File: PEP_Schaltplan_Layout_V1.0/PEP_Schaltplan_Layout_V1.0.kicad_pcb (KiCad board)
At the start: 2 copper layers, 202.5 x 119.7 mm, 115 parts, among them Q1 BC546, Q2 BC556, SW1 SW_DIP_x04, SW10 SW_DIP_x04, SW11 SW_DIP_x04, SW12 SW_DIP_x04, SW13 SW_DIP_x04, SW14 SW_DIP_x04, SW15 SW_DIP_x04, SW16 SW_DIP_x04, SW2 SW_DIP_x04, SW3 SW_DIP_x04, SW4 SW_DIP_x04, SW5 SW_DIP_x04, SW6 SW_DIP_x04, SW7 SW_DIP_x04, SW8 SW_DIP_x04, SW9 SW_DIP_x04, U1 AD822ANZ_new, U2 LM7805_TO220, U3 LM7905_TO220, U4 LT1819, U5 LT1819, U6 LT1819, U7 LT1819

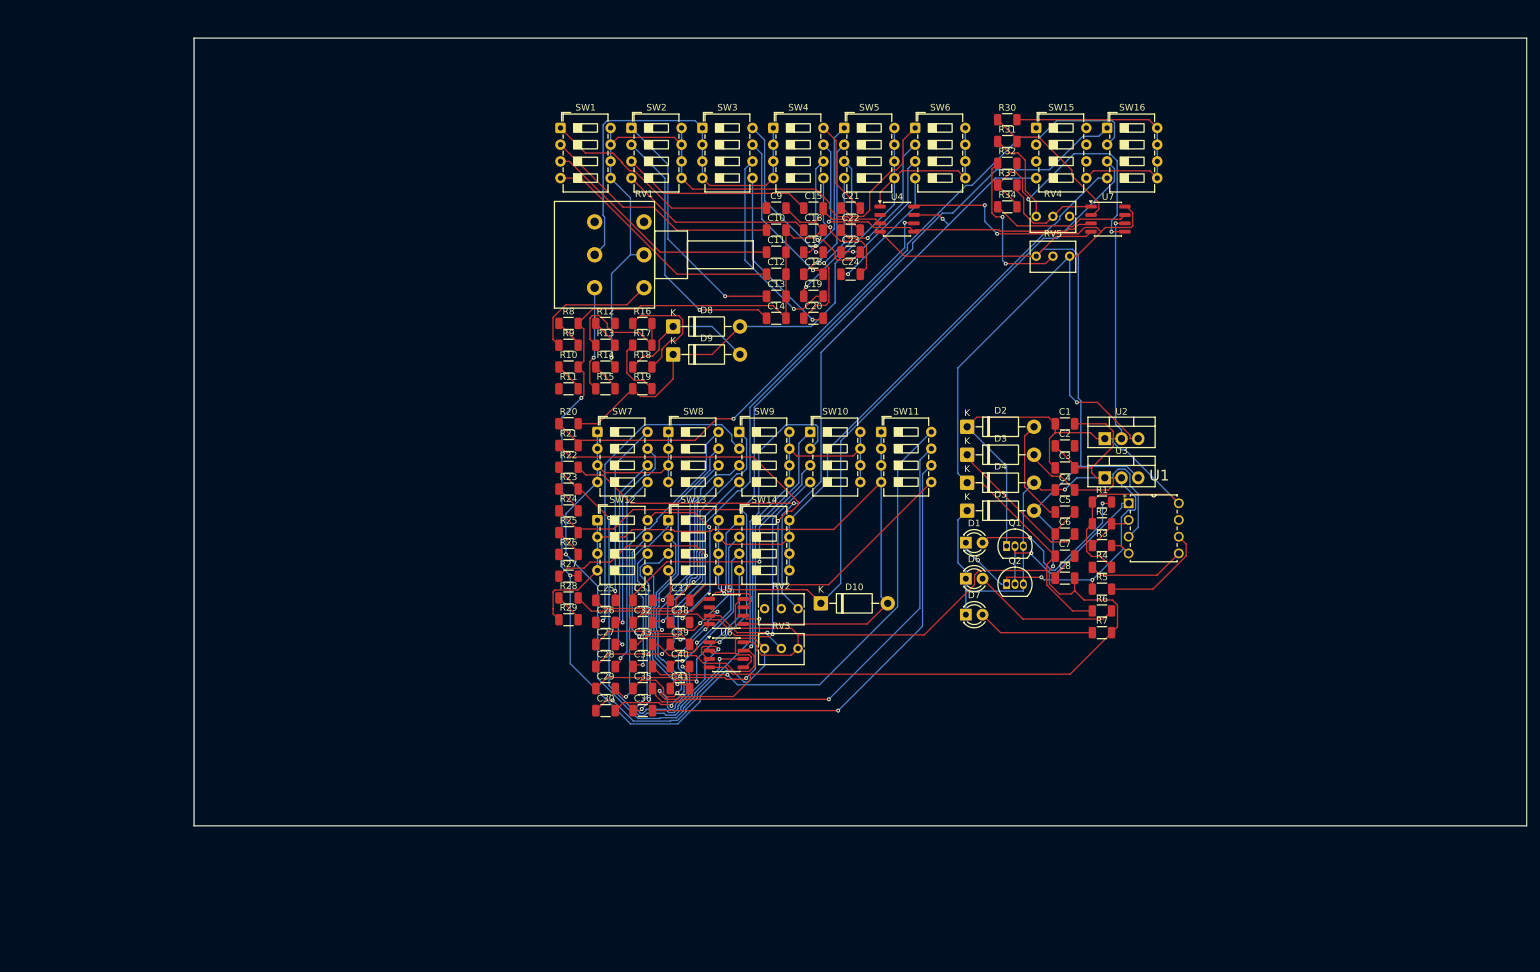
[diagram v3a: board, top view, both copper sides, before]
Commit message: Pinheads eingefügt, GND überall (hoffentlich angebunden)
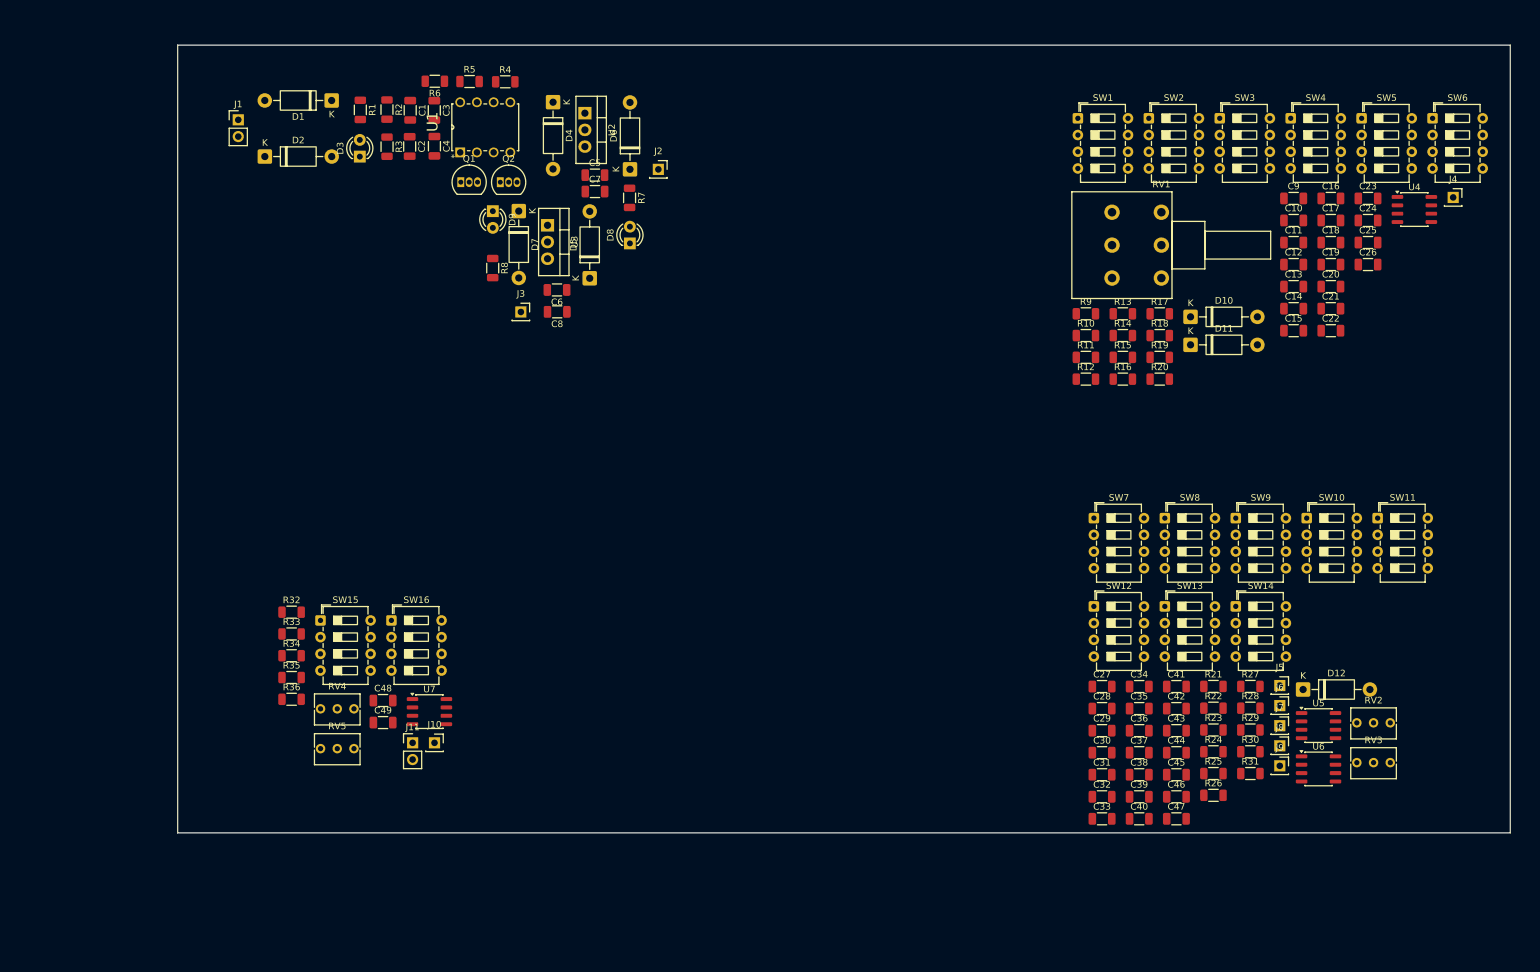
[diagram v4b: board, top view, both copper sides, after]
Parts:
- added C42: 220p, Capacitor_SMD:C_1206_3216Metric, F.Cu at (198.0, 142.6)
- added C43: 47p, Capacitor_SMD:C_1206_3216Metric, F.Cu at (198.0, 145.9)
- added C44: 47p, Capacitor_SMD:C_1206_3216Metric, F.Cu at (198.0, 149.3)
- added C45: 22p, Capacitor_SMD:C_1206_3216Metric, F.Cu at (198.0, 152.6)
- added C46: 0, Capacitor_SMD:C_1206_3216Metric, F.Cu at (198.0, 156.0)
- added C47: 0, Capacitor_SMD:C_1206_3216Metric, F.Cu at (198.0, 159.3)
- added C48: 100n, Capacitor_SMD:C_1206_3216Metric, F.Cu at (77.4, 141.3)
- added C49: 100n, Capacitor_SMD:C_1206_3216Metric, F.Cu at (77.4, 144.7)
- added D11: 1N4148, Diode_THT:D_DO-41_SOD81_P10.16mm_Horizontal, F.Cu at (200.2, 87.3)
- added D12: 1N4148, Diode_THT:D_DO-41_SOD81_P10.16mm_Horizontal, F.Cu at (217.3, 139.7)
- added J1: Conn_01x02_Pin, Connector_PinHeader_2.54mm:PinHeader_1x02_P2.54mm_Vertical, F.Cu at (55.4, 53.1)
- added J10: Conn_01x01_Pin, Connector_PinSocket_2.54mm:PinSocket_1x01_P2.54mm_Vertical, F.Cu at (85.3, 147.8)
- added J11: Conn_01x02_Pin, Connector_PinHeader_2.54mm:PinHeader_1x02_P2.54mm_Vertical, F.Cu at (81.9, 147.8)
- added J2: Conn_01x01_Pin, Connector_PinSocket_2.54mm:PinSocket_1x01_P2.54mm_Vertical, F.Cu at (119.3, 60.6)
- added J3: Conn_01x01_Pin, Connector_PinSocket_2.54mm:PinSocket_1x01_P2.54mm_Vertical, F.Cu at (98.4, 82.3)
- added J4: Conn_01x01_Pin, Connector_PinSocket_2.54mm:PinSocket_1x01_P2.54mm_Vertical, F.Cu at (240.1, 64.9)
- added J5: Conn_01x01_Pin, Connector_PinSocket_2.54mm:PinSocket_1x01_P2.54mm_Vertical, F.Cu at (213.7, 139.1)
- added J6: Conn_01x01_Pin, Connector_PinSocket_2.54mm:PinSocket_1x01_P2.54mm_Vertical, F.Cu at (213.7, 142.1)
- added J7: Conn_01x01_Pin, Connector_PinSocket_2.54mm:PinSocket_1x01_P2.54mm_Vertical, F.Cu at (213.7, 145.2)
- added J8: Conn_01x01_Pin, Connector_PinSocket_2.54mm:PinSocket_1x01_P2.54mm_Vertical, F.Cu at (213.7, 148.2)
- added J9: Conn_01x01_Pin, Connector_PinSocket_2.54mm:PinSocket_1x01_P2.54mm_Vertical, F.Cu at (213.7, 151.3)
- added R35: 10k, Resistor_SMD:R_1206_3216Metric, F.Cu at (63.5, 137.8)
- added R36: 10k, Resistor_SMD:R_1206_3216Metric, F.Cu at (63.5, 141.1)
- C10, C9: value 6.8n -> 100n
- C25: value 22n -> 6.8n
- C26: value 4.7n -> 6.8n
- C27: value 470p -> 100n
- C28: value 100p -> 100n
- C29: value 47p -> 100n
- C30: value 22p -> 100n
- C31: value 0 -> 22n
- C32, C40: value 0 -> 4.7n
- C33: value 1µ -> 470p
- C34: value 4.7n -> 100p
- C35: value 1n -> 47p
- C36: value 220p -> 22p
- C37, C38: value 47p -> 0
- C39: value 22p -> 1µ
- C41: value 0 -> 1n
- D1, D6, D7: value LED -> 1N4002; footprint LED_THT:LED_D3.0mm -> Diode_THT:D_DO-41_SOD81_P10.16mm_Horizontal
- D3: value 1N4002 -> LED; footprint Diode_THT:D_DO-41_SOD81_P10.16mm_Horizontal -> LED_THT:LED_D3.0mm
- D8, D9: value 1N4148 -> LED; footprint Diode_THT:D_DO-41_SOD81_P10.16mm_Horizontal -> LED_THT:LED_D3.0mm
- R11, R13: value 10k -> 0
- R12, R24: value 0 -> 10k
- R14: value 500 -> 10k
- R15, R9: value 0 -> 500
- R16: value 24K -> 0
- R17: value 12k -> 24K
- R18: value 0 -> 12k
- R20: value 1k -> 0
- R22, R32, R33: value 10k -> 1k
- R23: value 190k -> 0R
- R25: value 0 -> 190k
- R26: value 18k -> 0
- R27: value 100k -> 0
- R28: value 12k -> 18k
- R29: value ^0 -> 100k
- R30: value 1k -> 12k
- R31: value 1k -> ^0
- R6: value 470 -> 10k
- R8: value 500 -> 470
- moved RV4 132.0 mm to (73.0, 142.6)
- moved RV5 132.0 mm to (73.0, 148.6)
- moved SW16 132.0 mm to (78.7, 129.2)
- moved SW15 132.0 mm to (67.9, 129.2)
- moved R6 129.5 mm to (85.3, 47.2), turned to 180 degrees
- moved R32 128.4 mm to (63.5, 127.9)
- moved R33 128.4 mm to (63.5, 131.2)
- moved R34 128.4 mm to (63.5, 134.5)
- moved C25 128.0 mm to (227.1, 71.7)
- moved C26 128.0 mm to (227.1, 75.1)
- moved R1 127.5 mm to (74.0, 51.6), turned to -90 degrees
- moved U7 127.4 mm to (84.5, 143.0)
- moved R2 125.6 mm to (78.0, 51.5), turned to -90 degrees
- moved R3 124.4 mm to (78.0, 57.2), turned to -90 degrees
- moved R5 123.2 mm to (90.6, 47.3)
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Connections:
- C10 pad 1: Net-(C10-Pad1) -> -5V
- C17 pad 2: Net-(C17-Pad2) -> 0
- C18 pad 2: Net-(C18-Pad2) -> 0
- C2 pad 2: unconnected-(C2-Pad2) -> -7.5V
- C27 pad 1: Net-(C27-Pad1) -> +5V
- C27 pad 2: Net-(C27-Pad2) -> 0
- C28 pad 1: Net-(C28-Pad1) -> -5V
- C28 pad 2: Net-(C28-Pad2) -> 0
- C29 pad 1: Net-(C29-Pad1) -> +5V
- C29 pad 2: Net-(C29-Pad2) -> 0
- C30 pad 1: Net-(C30-Pad1) -> -5V
- C30 pad 2: Net-(C30-Pad2) -> 0
- C33 pad 1: Dreieck -> Net-(C33-Pad1)
- C39 pad 1: Net-(C39-Pad1) -> Dreieck
- C5 pad 1: Net-(D2-A) -> +5V
- C5 pad 2: Net-(C5-Pad2) -> GND
- C6 pad 1: Net-(C5-Pad2) -> GND
- C6 pad 2: Net-(D3-K) -> -5V
- C7 pad 2: Net-(C7-Pad2) -> GND
- C8 pad 1: Net-(C7-Pad2) -> GND
- C9 pad 1: Net-(C9-Pad1) -> +5V
- D1 pad 1: -7.5V -> +7.5V
- D10 pad 1: PWM -> Net-(D10-+)
- D10 pad 2: Net-(D10--) -> Sinus_Wien
- D2 pad 1: +7.5V -> Net-(D2-K)
- D2 pad 2: Net-(D2-A) -> -7.5V
- D3 pad 1: Net-(D3-K) -> -7.5V
- D3 pad 2: -7.5V -> Net-(D3-A)
- D4 pad 1: +5V -> +7.5V
- D4 pad 2: GND -> +5V
- D5 pad 1: GND -> -5V
- D5 pad 2: -5V -> -7.5V
- D6 pad 1: GND -> +5V
- D6 pad 2: Net-(D6-A) -> GND
- D7 pad 2: Net-(D7-A) -> -5V
- D8 pad 1: Net-(D8-+) -> GND
- D8 pad 2: Sinus_Wien -> Net-(D8-A)
- D9 pad 1: Sinus_Wien -> GND
- D9 pad 2: Net-(D8-+) -> Net-(D9-A)
- R1 pad 2: Net-(D1-A) -> Net-(D3-A)
- R10 pad 2: 0 -> Net-(R10-Pad2)
- R11 pad 1: Net-(U4A--) -> Net-(R11-Pad1)
- R11 pad 2: Net-(R10-Pad1) -> 0
- R12 pad 1: Net-(R12-Pad1) -> Net-(U4A--)
- R12 pad 2: Net-(U4A--) -> Net-(R11-Pad1)
- R13 pad 2: Net-(R12-Pad1) -> Net-(U4A--)
- R14 pad 2: Net-(U4A-+) -> Net-(R13-Pad1)
- R15 pad 2: Net-(R14-Pad1) -> Net-(U4A-+)
- R16 pad 2: Net-(R13-Pad1) -> Net-(R15-Pad1)
- R17 pad 2: Net-(R13-Pad1) -> Net-(R14-Pad1)
- R18 pad 1: Net-(D8-+) -> Net-(R18-Pad1)
- R18 pad 2: Net-(R16-Pad1) -> Net-(R14-Pad1)
- R19 pad 1: Sinus_Wien -> Net-(D10-+)
- R20 pad 1: Net-(U4B--) -> Sinus_Wien
- R20 pad 2: Sinus_Wien -> Net-(R18-Pad1)
- R21 pad 1: Net-(R21-Pad1) -> Net-(U4B--)
- R21 pad 2: Net-(U4B--) -> Sinus_Wien
- R22 pad 1: Net-(U6A-+) -> Net-(R22-Pad1)
- R22 pad 2: Sinus -> Net-(U4B--)
- R23 pad 2: Net-(U6A-+) -> Sinus
- R24 pad 1: Rechteck -> Net-(U6A-+)
- R25 pad 2: Rechteck -> Net-(U6A-+)
- R26 pad 1: Net-(U6B--) -> Rechteck
- R27 pad 1: Dreieck -> Net-(R27-Pad1)
- R27 pad 2: 0 -> Rechteck
- R28 pad 1: Net-(R28-Pad1) -> Net-(U6B--)
- R28 pad 2: PWM -> Net-(R27-Pad1)
- R29 pad 1: Net-(D10--) -> Dreieck
- R29 pad 2: Net-(R28-Pad1) -> 0
- R30 pad 1: Net-(U7A--) -> Net-(R30-Pad1)
- R30 pad 2: Net-(R30-Pad2) -> PWM
- R31 pad 1: Net-(R31-Pad1) -> Net-(D12--)
- R31 pad 2: Net-(U7A--) -> Net-(R30-Pad1)
- R32 pad 1: Net-(R32-Pad1) -> Net-(U7A--)
- R32 pad 2: Net-(U7B-+) -> Net-(R32-Pad2)
- R33 pad 1: Net-(U7B-+) -> Net-(R33-Pad1)
- R33 pad 2: Net-(R33-Pad2) -> Net-(U7A--)
- R34 pad 1: offset -> Net-(R34-Pad1)
- R4 pad 2: +7.5V -> -7.5V
- R5 pad 1: -7.5V -> +7.5V
- R6 pad 1: +5V -> Net-(R6-Pad1)
- R6 pad 2: Net-(D6-A) -> GND
- R7 pad 1: Net-(D7-A) -> +5V
- R7 pad 2: -5V -> Net-(D8-A)
- R8 pad 1: Net-(R8-Pad1) -> Net-(D9-A)
- R8 pad 2: 0 -> -5V
- R9 pad 1: Net-(R9-Pad1) -> Net-(R10-Pad2)
- R9 pad 2: Net-(R8-Pad1) -> 0
- RV1 pad 1: Net-(R9-Pad1) -> Net-(R10-Pad1)
- RV1 pad 4: Net-(R15-Pad1) -> Net-(R16-Pad1)
- RV2 pad 2: Net-(R21-Pad1) -> Net-(R22-Pad1)
- RV4 pad 2: Net-(R33-Pad2) -> Net-(J10-Pin_1)
- RV4 pad 3: Net-(R31-Pad1) -> Net-(R33-Pad1)
- RV5 pad 2: Net-(R32-Pad1) -> Net-(R34-Pad1)
- SW1 pad 1: Net-(C9-Pad1) -> Net-(C11-Pad1)
- SW1 pad 2: Net-(C10-Pad1) -> Net-(C12-Pad1)
- SW1 pad 3: Net-(C11-Pad1) -> Net-(C13-Pad1)
- SW1 pad 4: Net-(C12-Pad1) -> Net-(C14-Pad1)
- SW10 pad 1: Net-(C29-Pad1) -> Net-(C35-Pad1)
- SW10 pad 2: Net-(C30-Pad1) -> Net-(C36-Pad1)
- SW10 pad 3: Net-(C31-Pad1) -> Net-(C37-Pad1)
- SW10 pad 4: Net-(C32-Pad1) -> Net-(C38-Pad1)
- SW10 pad 5: Net-(C33-Pad2) -> Net-(C39-Pad2)
- SW10 pad 6: Net-(C33-Pad2) -> Net-(C39-Pad2)
- SW10 pad 7: Net-(C33-Pad2) -> Net-(C39-Pad2)
- SW10 pad 8: Net-(C33-Pad2) -> Net-(C39-Pad2)
- SW11 pad 1: Net-(D10--) -> Net-(D12--)
- SW11 pad 2: Net-(D10--) -> Net-(D12--)
- SW11 pad 3: Net-(D10--) -> Net-(D12--)
- SW11 pad 4: Net-(D10--) -> Net-(D12--)
- SW11 pad 5: Net-(C37-Pad2) -> Net-(C43-Pad2)
- SW11 pad 6: Net-(C36-Pad2) -> Net-(C42-Pad2)
- SW11 pad 7: Net-(C35-Pad2) -> Net-(C41-Pad2)
- SW11 pad 8: Net-(C34-Pad2) -> Net-(C40-Pad2)
- SW12 pad 1: Net-(D10--) -> Net-(D12--)
- SW12 pad 2: Net-(D10--) -> Net-(D12--)
- SW12 pad 3: Net-(D10--) -> Net-(D12--)
- SW12 pad 4: Net-(D10--) -> Net-(D12--)
- SW12 pad 5: Net-(C41-Pad2) -> Net-(C47-Pad2)
- SW12 pad 6: Net-(C40-Pad2) -> Net-(C46-Pad2)
- SW12 pad 7: Net-(C39-Pad2) -> Net-(C45-Pad2)
- SW12 pad 8: Net-(C38-Pad2) -> Net-(C44-Pad2)
- SW13 pad 1: Net-(C34-Pad1) -> Net-(C40-Pad1)
- SW13 pad 2: Net-(C35-Pad1) -> Net-(C41-Pad1)
- SW13 pad 3: Net-(C36-Pad1) -> Net-(C42-Pad1)
- SW13 pad 4: Net-(C37-Pad1) -> Net-(C43-Pad1)
- SW14 pad 1: Net-(C38-Pad1) -> Net-(C44-Pad1)
- SW14 pad 2: Net-(C39-Pad1) -> Net-(C45-Pad1)
- SW14 pad 3: Net-(C40-Pad1) -> Net-(C46-Pad1)
- SW14 pad 4: Net-(C41-Pad1) -> Net-(C47-Pad1)
- SW15 pad 5: Net-(R30-Pad2) -> Net-(R32-Pad2)
- SW16 pad 5: Net-(R30-Pad2) -> Net-(R32-Pad2)
- SW16 pad 6: Net-(R30-Pad2) -> Net-(R32-Pad2)
- SW16 pad 7: Net-(R30-Pad2) -> Net-(R32-Pad2)
- SW16 pad 8: Net-(R30-Pad2) -> Net-(R32-Pad2)
- SW2 pad 1: Net-(C13-Pad1) -> Net-(C15-Pad1)
- SW2 pad 2: Net-(C14-Pad1) -> Net-(C16-Pad1)
- SW2 pad 3: Net-(C15-Pad1) -> Net-(C17-Pad1)
- SW2 pad 4: Net-(C16-Pad1) -> Net-(C18-Pad1)
- SW3 pad 5: Net-(C20-Pad2) -> Net-(C22-Pad2)
- SW3 pad 6: Net-(C19-Pad2) -> Net-(C21-Pad2)
- SW3 pad 7: Net-(C18-Pad2) -> Net-(C20-Pad2)
- SW3 pad 8: Net-(C17-Pad2) -> Net-(C19-Pad2)
- SW4 pad 5: Net-(C24-Pad2) -> Net-(C26-Pad2)
- SW4 pad 6: Net-(C23-Pad2) -> Net-(C25-Pad2)
- SW4 pad 7: Net-(C22-Pad2) -> Net-(C24-Pad2)
- SW4 pad 8: Net-(C21-Pad2) -> Net-(C23-Pad2)
- SW5 pad 1: Net-(C17-Pad1) -> Net-(C19-Pad1)
- SW5 pad 2: Net-(C18-Pad1) -> Net-(C20-Pad1)
- SW5 pad 3: Net-(C19-Pad1) -> Net-(C21-Pad1)
- SW5 pad 4: Net-(C20-Pad1) -> Net-(C22-Pad1)
- SW6 pad 1: Net-(C21-Pad1) -> Net-(C23-Pad1)
- SW6 pad 2: Net-(C22-Pad1) -> Net-(C24-Pad1)
- SW6 pad 3: Net-(C23-Pad1) -> Net-(C25-Pad1)
- SW6 pad 4: Net-(C24-Pad1) -> Net-(C26-Pad1)
- SW7 pad 5: Net-(C28-Pad2) -> Net-(C34-Pad2)
- SW7 pad 6: Net-(C27-Pad2) -> Net-(C33-Pad2)
- SW7 pad 7: Net-(C26-Pad2) -> Net-(C32-Pad2)
- SW7 pad 8: Net-(C25-Pad2) -> Net-(C31-Pad2)
- SW8 pad 5: Net-(C32-Pad2) -> Net-(C38-Pad2)
- SW8 pad 6: Net-(C31-Pad2) -> Net-(C37-Pad2)
- SW8 pad 7: Net-(C30-Pad2) -> Net-(C36-Pad2)
- SW8 pad 8: Net-(C29-Pad2) -> Net-(C35-Pad2)
- SW9 pad 1: Net-(C25-Pad1) -> Net-(C31-Pad1)
- SW9 pad 2: Net-(C26-Pad1) -> Net-(C32-Pad1)
- SW9 pad 3: Net-(C27-Pad1) -> Net-(C33-Pad1)
- SW9 pad 4: Net-(C28-Pad1) -> Net-(C34-Pad1)
- SW9 pad 5: Net-(C33-Pad2) -> Net-(C39-Pad2)
- SW9 pad 6: Net-(C33-Pad2) -> Net-(C39-Pad2)
- SW9 pad 7: Net-(C33-Pad2) -> Net-(C39-Pad2)
- SW9 pad 8: Net-(C33-Pad2) -> Net-(C39-Pad2)
- U1 pad 7: unconnected-(U1-Pad7) -> Net-(R6-Pad1)
- U5 pad 5: Net-(D10--) -> Net-(D12--)
- U6 pad 7: Net-(C33-Pad2) -> Net-(C39-Pad2)
- U7 pad 1: Net-(R33-Pad2) -> Net-(J10-Pin_1)
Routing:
- net 0: track 227.0 -> 0.00 mm, vias 3 -> 0
- net -5V: track 226.5 -> 0.00 mm, vias 3 -> 0
- net +5V: track 225.2 -> 0.00 mm, vias 3 -> 0
- net Dreieck: track 159.9 -> 0.00 mm, vias 3 -> 0
- net Rechteck: track 142.4 -> 0.00 mm, vias 2 -> 0
- net GND: track 129.6 -> 0.00 mm, vias 2 -> 0
- net Sinus: track 127.5 -> 0.00 mm, vias 2 -> 0
- net PWM: track 127.3 -> 0.00 mm
- net Net-(D10--): track 116.8 -> 0.00 mm
- net Sägezahn: track 110.3 -> 0.00 mm, vias 1 -> 0
- net Sinus_Wien: track 104.7 -> 0.00 mm
- net Net-(U4A-+): track 93.9 -> 0.00 mm, vias 1 -> 0
- net +7.5V: track 92.8 -> 0.00 mm
- net Net-(U6B--): track 91.6 -> 0.00 mm, vias 2 -> 0
- net Net-(C33-Pad2): track 76.8 -> 0.00 mm, vias 1 -> 0
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
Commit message: Widerstand eingefügt um Notfall Sinus extern, einzuspeisen
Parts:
- added R37: 0R, Resistor_SMD:R_1206_3216Metric, F.Cu at (201.5, 92.6)
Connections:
- R21 pad 2: Sinus_Wien -> Net-(R21-Pad2)
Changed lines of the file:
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@@
 		)
 	)
+	(footprint "Resistor_SMD:R_1206_3216Metric"
+		(layer "F.Cu")
+		(at 201.518559 92.625226)
+		(descr "Resistor SMD 1206 (3216 Metric), square (rectangular) end terminal, IPC-7351 nominal, (Body size source: IPC-SM-782 page 72, https://www.pcb-3d.com/wordpress/wp-content/uploads/ipc-sm-782a_amendment_1_and_2.pdf)")
+		(tags "resistor")
+		(property "Reference" "R37"
+			(at 0 -1.83 0)
+			(layer "F.SilkS")
+			(effects
+				(font
+					(size 1 1)
+					(thickness 0.15)
+				)
+			)
+		)
+		(property "Value" "0R"
+			(at 0 1.83 0)
+			(layer "F.Fab")
+			(effects
+				(font
+					(size 1 1)
+					(thickness 0.15)
+				)
+			)
+		)
+		(property "Datasheet" ""
+			(at 0 0 0)
+			(layer "F.Fab")
+			(hide yes)
+			(effects
+				(font
+					(size 1.27 1.27)
+				)
+			)
+		)
+		(property "Description" ""
+			(at 0 0 0)
+			(layer "F.Fab")
+			(hide yes)
+			(effects
+				(font
+					(size 1.27 1.27)
+				)
+			)
+		)
+		(property "Sim.Device" "R"
+			(at 0 0 0)
+			(unlocked yes)
+			(layer "F.Fab")
+			(hide yes)
+			(effects
+				(font
+					(size 1 1)
+					(thickness 0.15)
+				)
+			)
+		)
+		(property "Sim.Params" "R=0R"
+			(at 0 0 0)
+			(unlocked yes)
+			(layer "F.Fab")
+			(hide yes)
+			(effects
+				(font
+					(size 1 1)
+					(thickness 0.15)
+				)
+			)
+		)
+		(sheetname "/Signalverarebeitung/")
+		(sheetfile "Signalverarebeitung.kicad_sch")
+		(units
+			(unit
+				(name "A")
+				(pins "1" "2")
+			)
+		)
+		(attr smd)
+		(duplicate_pad_numbers_are_jumpers no)
+		(fp_line
+			(start -0.727064 -0.91)
+			(end 0.727064 -0.91)
+			(stroke
+				(width 0.12)
+				(type solid)
+			)
+			(layer "F.SilkS")
+		)
+		(fp_line
+			(start -0.727064 0.91)
+			(end 0.727064 0.91)
+			(stroke
+				(width 0.12)
+				(type solid)
+			)
+			(layer "F.SilkS")
+		)
+		(fp_rect
+			(start -2.28 -1.13)
+			(end 2.28 1.13)
+			(stroke
+				(width 0.05)
+				(type solid)
+			)
+			(fill no)
+			(layer "F.CrtYd")
+		)
+		(fp_rect
+			(start -1.6 -0.8)
+			(end 1.6 0.8)
+			(stroke
+				(width 0.1)
+				(type solid)
+			)
+			(fill no)
+			(layer "F.Fab")
+		)
+		(fp_text user "${REFERENCE}"
+			(at 0 0 0)
+			(layer "F.Fab")
+			(effects
+				(font
+					(size 0.8 0.8)
+					(thickness 0.12)
+				)
+			)
+		)
+		(pad "1" smd roundrect
+			(at -1.4625 0)
+			(size 1.125 1.75)
+			(layers "F.Cu" "F.Mask" "F.Paste")
+			(roundrect_rratio 0.222222)
+			(net "Net-(R21-Pad2)")
+			(pintype "passive")
+		)
+		(pad "2" smd roundrect
+			(at 1.4625 0)
+			(size 1.125 1.75)
+			(layers "F.Cu" "F.Mask" "F.Paste")
+			(roundrect_rratio 0.222222)
+			(net "Sinus_Wien")
+			(pintype "passive")
+		)
+		(embedded_fonts no)
+		(model "${KICAD10_3DMODEL_DIR}/Resistor_SMD.3dshapes/R_1206_3216Metric.step"
+			(offset
+				(xyz 0 0 0)
+			)
+			(scale
+				(xyz 1 1 1)
+			)
+			(rotate
+				(xyz 0 0 0)
+			)
+		)
+	)
 	(footprint "Capacitor_SMD:C_1206_3216Metric"
 		(layer "F.Cu")
@@
 			(layers "F.Cu" "F.Mask" "F.Paste")
 			(roundrect_rratio 0.222222)
-			(net "Sinus_Wien")
+			(net "Net-(R21-Pad2)")
 			(pintype "passive")
 		)

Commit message: Hab den Pin zum einspeisen vergessen
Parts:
- added J12: Conn_01x01_Pin, Connector_PinSocket_2.54mm:PinSocket_1x01_P2.54mm_Vertical, F.Cu at (200.2, 96.5)
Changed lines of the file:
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@@
 			(layers "F.Cu" "F.Mask" "F.Paste")
 			(roundrect_rratio 0.222222)
-			(net "Net-(R21-Pad2)")
+			(net "Net-(J12-Pin_1)")
 			(pintype "passive")
 		)
@@
 		)
 	)
+	(footprint "Connector_PinSocket_2.54mm:PinSocket_1x01_P2.54mm_Vertical"
+		(layer "F.Cu")
+		(at 200.198559 96.455226)
+		(descr "Through hole straight socket strip, 1x01, 2.54mm pitch, single row (from Kicad 4.0.7), script generated")
+		(tags "Through hole socket strip THT 1x01 2.54mm single row")
+		(property "Reference" "J12"
+			(at 0 -2.77 0)
+			(layer "F.SilkS")
+			(effects
+				(font
+					(size 1 1)
+					(thickness 0.15)
+				)
+			)
+		)
+		(property "Value" "Conn_01x01_Pin"
+			(at 0 2.77 0)
+			(layer "F.Fab")
+			(effects
+				(font
+					(size 1 1)
+					(thickness 0.15)
+				)
+			)
+		)
+		(property "Datasheet" ""
+			(at 0 0 0)
+			(layer "F.Fab")
+			(hide yes)
+			(effects
+				(font
+					(size 1.27 1.27)
+				)
+			)
+		)
+		(property "Description" "Generic connector, single row, 01x01, script generated"
+			(at 0 0 0)
+			(layer "F.Fab")
+			(hide yes)
+			(effects
+				(font
+					(size 1.27 1.27)
+				)
+			)
+		)
+		(property ki_fp_filters "Connector*:*_1x??_*")
+		(sheetname "/Signalverarebeitung/")
+		(sheetfile "Signalverarebeitung.kicad_sch")
+		(units
+			(unit
+				(name "A")
+				(pins "1")
+			)
+		)
+		(attr through_hole)
+		(duplicate_pad_numbers_are_jumpers no)
+		(fp_line
+			(start -1.33 1.21)
+			(end -1.33 1.33)
+			(stroke
+				(width 0.12)
+				(type solid)
+			)
+			(layer "F.SilkS")
+		)
+		(fp_line
+			(start -1.33 1.33)
+			(end 1.33 1.33)
+			(stroke
+				(width 0.12)
+				(type solid)
+			)
+			(layer "F.SilkS")
+		)
+		(fp_line
+			(start 0 -1.33)
+			(end 1.33 -1.33)
+			(stroke
+				(width 0.12)
+				(type solid)
+			)
+			(layer "F.SilkS")
+		)
+		(fp_line
+			(start 1.33 -1.33)
+			(end 1.33 0)
+			(stroke
+				(width 0.12)
+				(type solid)
+			)
+			(layer "F.SilkS")
+		)
+		(fp_line
+			(start 1.33 1.21)
+			(end 1.33 1.33)
+			(stroke
+				(width 0.12)
+				(type solid)
+			)
+			(layer "F.SilkS")
+		)
+		(fp_line
+			(start -1.77 -1.77)
+			(end 1.77 -1.77)
+			(stroke
+				(width 0.05)
+				(type solid)
+			)
+			(layer "F.CrtYd")
+		)
+		(fp_line
+			(start -1.77 1.77)
+			(end -1.77 -1.77)
+			(stroke
+				(width 0.05)
+				(type solid)
+			)
+			(layer "F.CrtYd")
+		)
+		(fp_line
+			(start 1.77 -1.77)
+			(end 1.77 1.77)
+			(stroke
+				(width 0.05)
+				(type solid)
+			)
+			(layer "F.CrtYd")
+		)
+		(fp_line
+			(start 1.77 1.77)
+			(end -1.77 1.77)
+			(stroke
+				(width 0.05)
+				(type solid)
+			)
+			(layer "F.CrtYd")
+		)
+		(fp_line
+			(start -1.27 -1.27)
+			(end 0.635 -1.27)
+			(stroke
+				(width 0.1)
+				(type solid)
+			)
+			(layer "F.Fab")
+		)
+		(fp_line
+			(start -1.27 1.27)
+			(end -1.27 -1.27)
+			(stroke
+				(width 0.1)
+				(type solid)
+			)
+			(layer "F.Fab")
+		)
+		(fp_line
+			(start 0.635 -1.27)
+			(end 1.27 -0.635)
+			(stroke
+				(width 0.1)
+				(type solid)
+			)
+			(layer "F.Fab")
+		)
+		(fp_line
+			(start 1.27 -0.635)
+			(end 1.27 1.27)
+			(stroke
+				(width 0.1)
+				(type solid)
+			)
+			(layer "F.Fab")
+		)
+		(fp_line
+			(start 1.27 1.27)
+			(end -1.27 1.27)
+			(stroke
+				(width 0.1)
+				(type solid)
+			)
+			(layer "F.Fab")
+		)
+		(fp_text user "${REFERENCE}"
+			(at 0 0 0)
+			(layer "F.Fab")
+			(effects
+				(font
+					(size 1 1)
+					(thickness 0.15)
+				)
+			)
+		)
+		(pad "1" thru_hole rect
+			(at 0 0)
+			(size 1.7 1.7)
+			(drill 1)
+			(layers "*.Cu" "*.Mask")
+			(remove_unused_layers no)
+			(net "Net-(J12-Pin_1)")
+			(pinfunction "Pin_1_1")
+			(pintype "passive")
+		)
+		(embedded_fonts no)
+		(model "${KICAD10_3DMODEL_DIR}/Connector_PinSocket_2.54mm.3dshapes/PinSocket_1x01_P2.54mm_Vertical.step"
+			(offset
+				(xyz 0 0 0)
+			)
+			(scale
+				(xyz 1 1 1)
+			)
+			(rotate
+				(xyz 0 0 0)
+			)
+		)
+	)
 	(footprint "Resistor_SMD:R_1206_3216Metric"
 		(layer "F.Cu")
@@
 			(layers "F.Cu" "F.Mask" "F.Paste")
 			(roundrect_rratio 0.222222)
-			(net "Net-(R21-Pad2)")
+			(net "Net-(J12-Pin_1)")
 			(pintype "passive")
 		)

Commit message: Sortierung Signalverarbeitung +Offset & Amplitude
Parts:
- moved U4 181.7 mm to (62.8, 127.2)
- moved R36 171.7 mm to (235.2, 140.1), turned to -90 degrees
- moved RV2 162.8 mm to (68.3, 131.3), turned to 180 degrees
- moved R34 160.7 mm to (224.0, 143.2), turned to 90 degrees
- moved R35 160.4 mm to (224.0, 137.4), turned to 90 degrees
- moved J11 157.8 mm to (239.6, 141.4), turned to 180 degrees
- moved R32 156.3 mm to (219.1, 143.2), turned to -90 degrees
- moved R33 155.7 mm to (219.1, 137.4), turned to -90 degrees
- moved RV5 153.3 mm to (226.3, 149.9)
- moved RV4 151.7 mm to (224.3, 131.0)
- moved J5 149.1 mm to (64.8, 132.0), turned to 180 degrees
- moved U7 145.5 mm to (229.9, 140.2)
- moved J10 143.4 mm to (228.0, 134.0)
- moved R37 142.4 mm to (61.9, 120.3), turned to 180 degrees
- moved SW15 139.8 mm to (207.5, 122.8)
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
